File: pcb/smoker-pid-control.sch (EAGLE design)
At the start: 12 parts, among them SW1 EC12E_SW

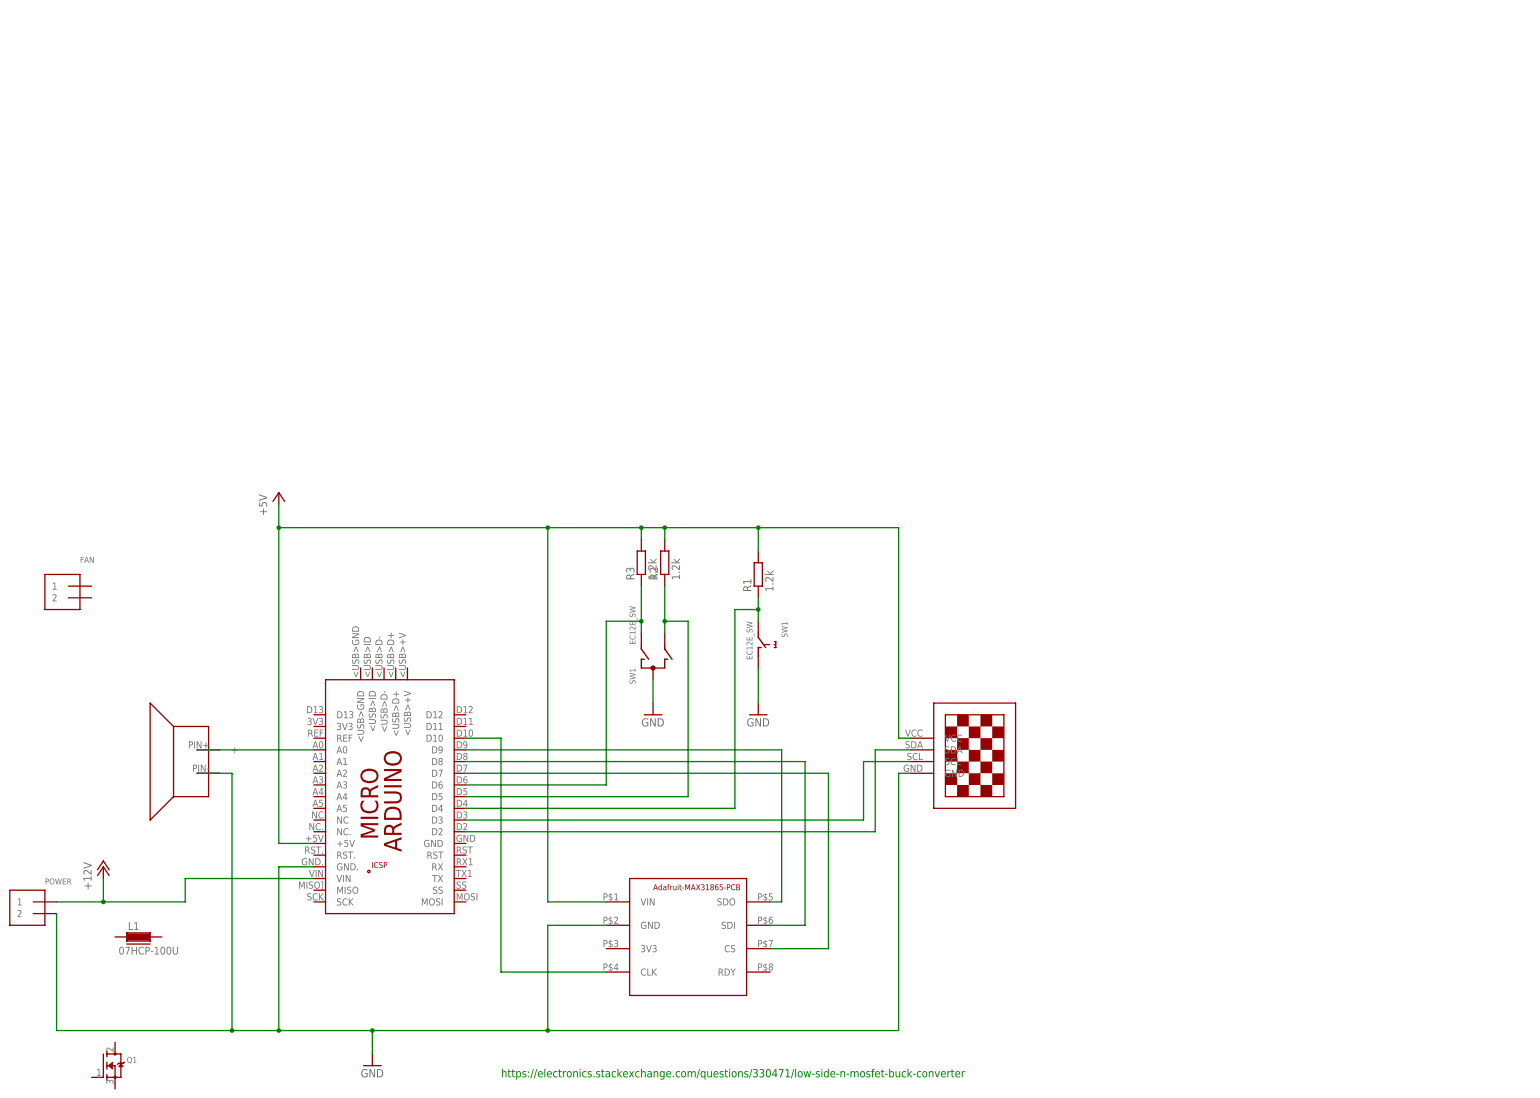
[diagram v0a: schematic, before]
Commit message: pcb with pulldown on gate
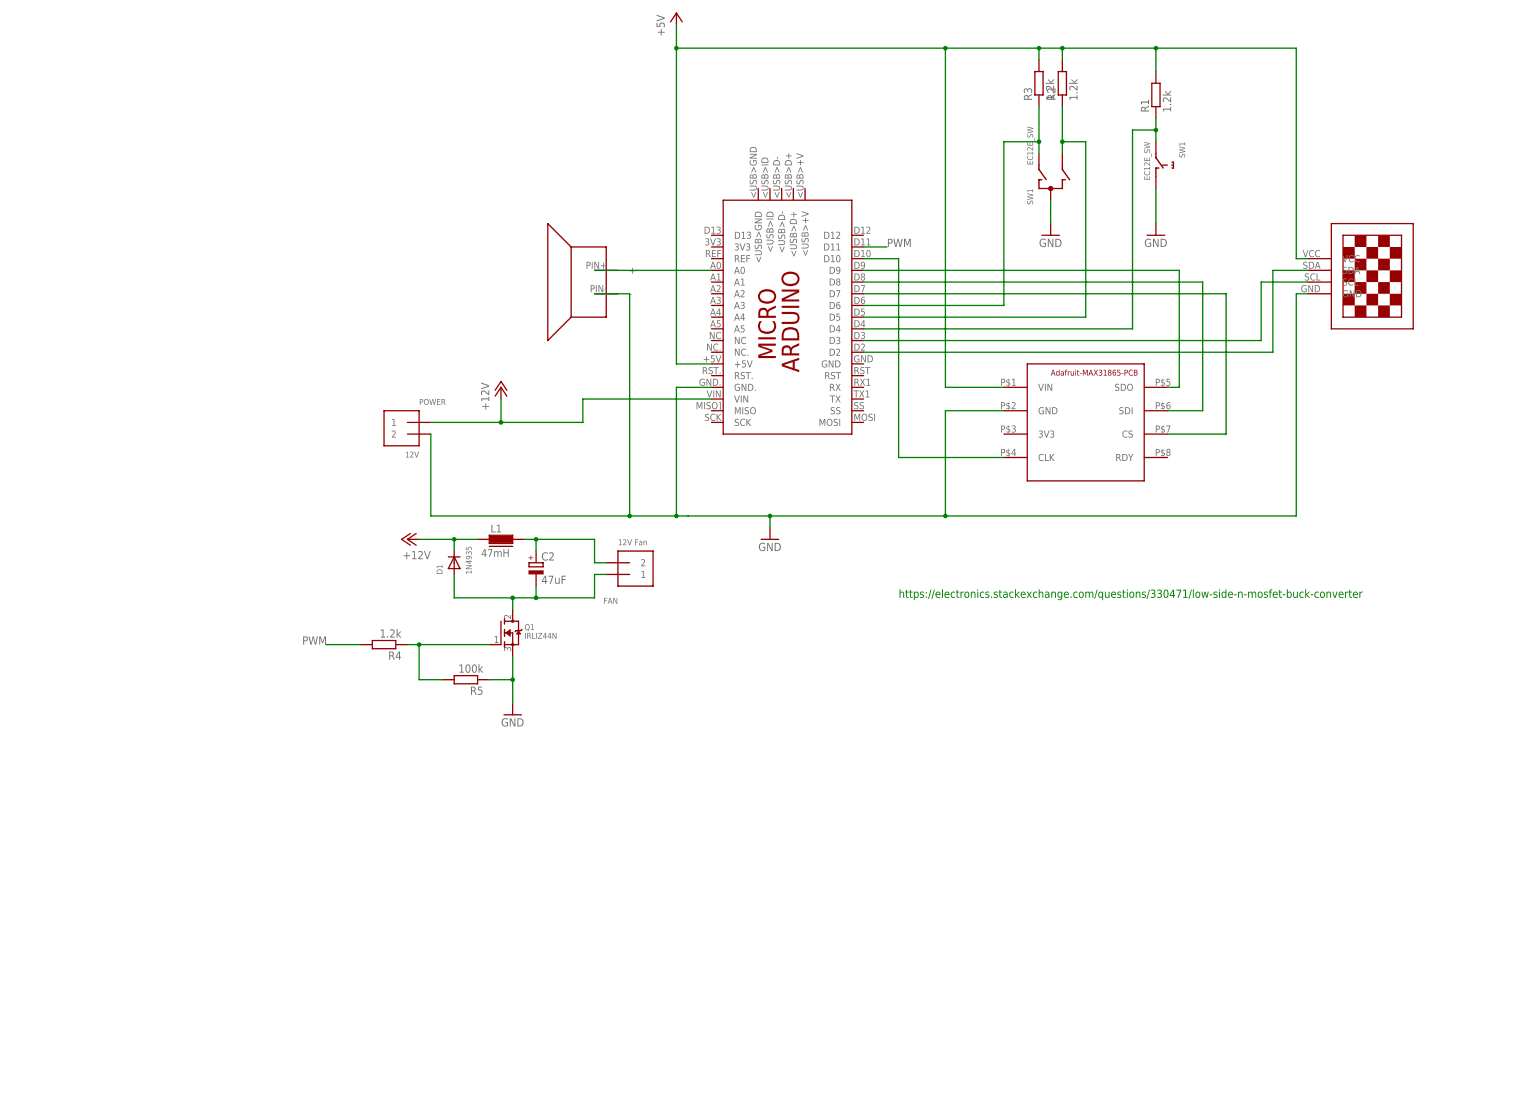
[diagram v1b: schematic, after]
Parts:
- added C2: 47uF, rcl:CPOL-EUE5-8.5
- added D1: 1N4935, adafruit:DIODEDO-1N4148
- added R4: 1.2k, rcl:R-EU_0207/10
- added R5: 100k, rcl:R-EU_0207/10
- FAN: value (none) -> 12V Fan
- L1: value 07HCP-100U -> 47mH
- POWER: value (none) -> 12V
- Q1: value (none) -> IRLIZ44N
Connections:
- new net N$11: C2.+, FAN.2, L1.2
- new net N$12: Q1.G, R4.1, R5.2
- new net N$14: C2.-, D1.A, FAN.1, Q1.D
- new net PWM: PCB1.D11, R4.2
- net +12V: now also D1.C, L1.1
- net GND: now also Q1.S, R5.1
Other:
- moved on the sheet: FAN, L1, POWER, Q1, R1, R2, R3, SW1

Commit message: fix drill hole sizes, fix oled wiring bug
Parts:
- R2: device rcl:R-EU_0207/10 -> rcl:R-EU_0207/15
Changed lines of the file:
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@@
 <grid distance="0.1" unitdist="inch" unit="inch" style="lines" multiple="1" display="no" altdistance="0.01" altunitdist="inch" altunit="inch"/>
 <layers>
-<layer number="1" name="Top" color="4" fill="1" visible="yes" active="no"/>
-<layer number="16" name="Bottom" color="1" fill="1" visible="yes" active="no"/>
-<layer number="17" name="Pads" color="2" fill="1" visible="yes" active="no"/>
-<layer number="18" name="Vias" color="2" fill="1" visible="yes" active="no"/>
-<layer number="19" name="Unrouted" color="6" fill="1" visible="yes" active="no"/>
-<layer number="20" name="Dimension" color="24" fill="1" visible="yes" active="no"/>
-<layer number="21" name="tPlace" color="7" fill="1" visible="yes" active="no"/>
-<layer number="22" name="bPlace" color="7" fill="1" visible="yes" active="no"/>
-<layer number="23" name="tOrigins" color="15" fill="1" visible="yes" active="no"/>
-<layer number="24" name="bOrigins" color="15" fill="1" visible="yes" active="no"/>
-<layer number="25" name="tNames" color="7" fill="1" visible="yes" active="no"/>
-<layer number="26" name="bNames" color="7" fill="1" visible="yes" active="no"/>
-<layer number="27" name="tValues" color="7" fill="1" visible="yes" active="no"/>
-<layer number="28" name="bValues" color="7" fill="1" visible="yes" active="no"/>
+<layer number="1" name="Top" color="4" fill="1" visible="no" active="no"/>
+<layer number="16" name="Bottom" color="1" fill="1" visible="no" active="no"/>
+<layer number="17" name="Pads" color="2" fill="1" visible="no" active="no"/>
+<layer number="18" name="Vias" color="2" fill="1" visible="no" active="no"/>
+<layer number="19" name="Unrouted" color="6" fill="1" visible="no" active="no"/>
+<layer number="20" name="Dimension" color="24" fill="1" visible="no" active="no"/>
+<layer number="21" name="tPlace" color="7" fill="1" visible="no" active="no"/>
+<layer number="22" name="bPlace" color="7" fill="1" visible="no" active="no"/>
+<layer number="23" name="tOrigins" color="15" fill="1" visible="no" active="no"/>
+<layer number="24" name="bOrigins" color="15" fill="1" visible="no" active="no"/>
+<layer number="25" name="tNames" color="7" fill="1" visible="no" active="no"/>
+<layer number="26" name="bNames" color="7" fill="1" visible="no" active="no"/>
+<layer number="27" name="tValues" color="7" fill="1" visible="no" active="no"/>
+<layer number="28" name="bValues" color="7" fill="1" visible="no" active="no"/>
 <layer number="29" name="tStop" color="7" fill="3" visible="no" active="no"/>
 <layer number="30" name="bStop" color="7" fill="6" visible="no" active="no"/>
@@
 <layer number="35" name="tGlue" color="7" fill="4" visible="no" active="no"/>
 <layer number="36" name="bGlue" color="7" fill="5" visible="no" active="no"/>
-<layer number="37" name="tTest" color="7" fill="1" visible="yes" active="no"/>
-<layer number="38" name="bTest" color="7" fill="1" visible="yes" active="no"/>
+<layer number="37" name="tTest" color="7" fill="1" visible="no" active="no"/>
+<layer number="38" name="bTest" color="7" fill="1" visible="no" active="no"/>
 <layer number="39" name="tKeepout" color="4" fill="11" visible="no" active="no"/>
 <layer number="40" name="bKeepout" color="1" fill="11" visible="no" active="no"/>
@@
 <layer number="44" name="Drills" color="7" fill="1" visible="no" active="no"/>
 <layer number="45" name="Holes" color="7" fill="1" visible="no" active="no"/>
-<layer number="46" name="Milling" color="3" fill="1" visible="yes" active="no"/>
-<layer number="47" name="Measures" color="7" fill="1" visible="yes" active="no"/>
-<layer number="48" name="Document" color="7" fill="1" visible="yes" active="no"/>
-<layer number="49" name="Reference" color="7" fill="1" visible="yes" active="no"/>
-<layer number="50" name="dxf" color="7" fill="1" visible="yes" active="no"/>
-<layer number="51" name="tDocu" color="7" fill="1" visible="yes" active="no"/>
-<layer number="52" name="bDocu" color="7" fill="1" visible="yes" active="no"/>
-<layer number="53" name="tGND_GNDA" color="7" fill="9" visible="yes" active="no"/>
-<layer number="54" name="bGND_GNDA" color="1" fill="9" visible="yes" active="no"/>
-<layer number="56" name="wert" color="7" fill="1" visible="yes" active="no"/>
-<layer number="57" name="tCAD" color="7" fill="1" visible="yes" active="no"/>
-<layer number="59" name="tCarbon" color="7" fill="1" visible="yes" active="no"/>
-<layer number="60" name="bCarbon" color="7" fill="1" visible="yes" active="no"/>
+<layer number="46" name="Milling" color="3" fill="1" visible="no" active="no"/>
+<layer number="47" name="Measures" color="7" fill="1" visible="no" active="no"/>
+<layer number="48" name="Document" color="7" fill="1" visible="no" active="no"/>
+<layer number="49" name="Reference" color="7" fill="1" visible="no" active="no"/>
+<layer number="50" name="dxf" color="7" fill="1" visible="no" active="no"/>
+<layer number="51" name="tDocu" color="7" fill="1" visible="no" active="no"/>
+<layer number="52" name="bDocu" color="7" fill="1" visible="no" active="no"/>
+<layer number="53" name="tGND_GNDA" color="7" fill="9" visible="no" active="no"/>
+<layer number="54" name="bGND_GNDA" color="1" fill="9" visible="no" active="no"/>
+<layer number="56" name="wert" color="7" fill="1" visible="no" active="no"/>
+<layer number="57" name="tCAD" color="7" fill="1" visible="no" active="no"/>
+<layer number="59" name="tCarbon" color="7" fill="1" visible="no" active="no"/>
+<layer number="60" name="bCarbon" color="7" fill="1" visible="no" active="no"/>
 <layer number="88" name="SimResults" color="9" fill="1" visible="yes" active="yes"/>
 <layer number="89" name="SimProbes" color="9" fill="1" visible="yes" active="yes"/>
@@
 <part name="R1" library="rcl" library_urn="urn:adsk.eagle:library:334" deviceset="R-EU_" device="0207/10" package3d_urn="urn:adsk.eagle:package:23491/2" value="1.2k"/>
 <part name="GND2" library="supply1" library_urn="urn:adsk.eagle:library:371" deviceset="GND" device=""/>
-<part name="R2" library="rcl" library_urn="urn:adsk.eagle:library:334" deviceset="R-EU_" device="0207/10" package3d_urn="urn:adsk.eagle:package:23491/2" value="1.2k"/>
+<part name="R2" library="rcl" library_urn="urn:adsk.eagle:library:334" deviceset="R-EU_" device="0207/15" package3d_urn="urn:adsk.eagle:package:23492/1" value="1.2k"/>
 <part name="R3" library="rcl" library_urn="urn:adsk.eagle:library:334" deviceset="R-EU_" device="0207/10" package3d_urn="urn:adsk.eagle:package:23491/2" value="1.2k"/>
 <part name="GND3" library="supply1" library_urn="urn:adsk.eagle:library:371" deviceset="GND" device=""/>
